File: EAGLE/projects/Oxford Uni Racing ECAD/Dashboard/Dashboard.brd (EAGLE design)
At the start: 165.1 x 153.3 mm, 18 parts, among them J1 T821108A1S100CEU, J2 CAN_OUT, J3 PWR_CAN, K1 EC2-12NU, K2 EC2-12NU, X2 D-SUB9-H2M09ST

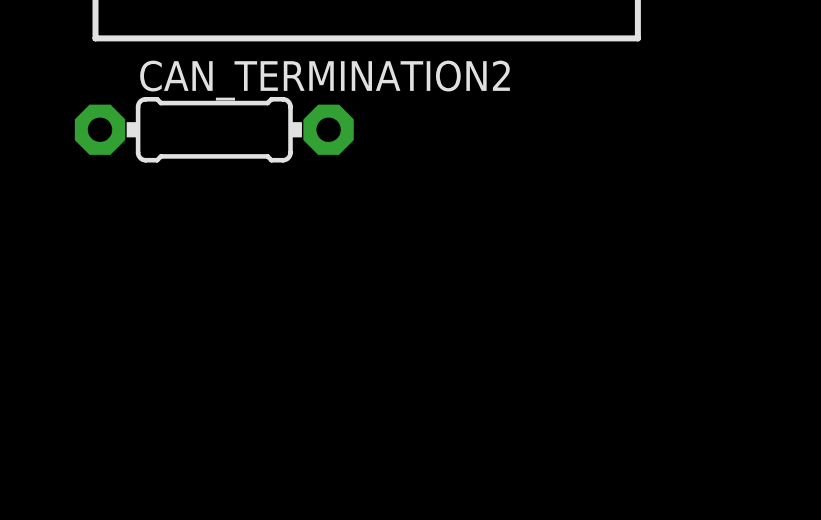
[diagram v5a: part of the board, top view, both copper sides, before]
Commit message: added DISPLAY OUT to dashboard
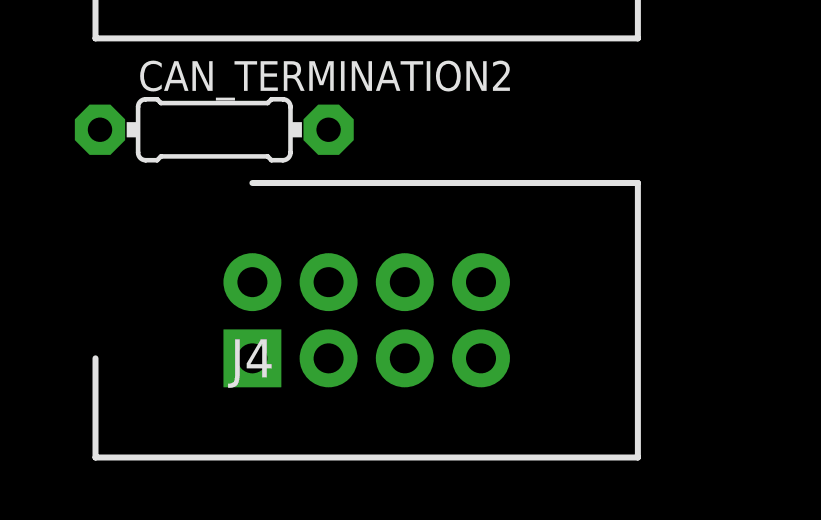
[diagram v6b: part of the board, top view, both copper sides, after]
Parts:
- added J4: DISPL, T821108A1S100CEU:HDRV8W64P254_2X4_1778X895X915P
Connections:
- new net DISPL_SCL: J4.7
- new net DISPL_SDA: J4.5
- net 5V: now also J4.1
- net GND: now also J4.3
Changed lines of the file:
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@@
 <attribute name="VALUE" x="6.35" y="-45.72" size="1.27" layer="27" align="center"/>
+</element>
+<element name="J4" library="T821108A1S100CEU" package="HDRV8W64P254_2X4_1778X895X915P" value="DISPL" x="6.35" y="-59.69" smashed="yes">
+<attribute name="DESCRIPTION" value="HEADER, VERTICAL, 2.54MM, 8WAY Amphenol T821 Series, 2.54mm Pitch 8 Way 2 Row Straight PCB Header, Solder Termination, 3A" x="6.35" y="-59.69" size="1.778" layer="27" display="off"/>
+<attribute name="HEIGHT" value="9.15mm" x="6.35" y="-59.69" size="1.778" layer="27" display="off"/>
+<attribute name="MANUFACTURER_NAME" value="Amphenol" x="6.35" y="-59.69" size="1.778" layer="27" display="off"/>
+<attribute name="MANUFACTURER_PART_NUMBER" value="T821108A1S100CEU" x="6.35" y="-59.69" size="1.778" layer="27" display="off"/>
+<attribute name="NAME" x="6.35" y="-59.69" size="1.27" layer="25" align="center"/>
+<attribute name="RS_PART_NUMBER" value="1702738" x="6.35" y="-59.69" size="1.778" layer="27" display="off"/>
+<attribute name="VALUE" x="6.35" y="-59.69" size="1.27" layer="27" align="center"/>
 </element>
 </elements>
@@
 <contactref element="J2" pad="4"/>
 <contactref element="J2" pad="3"/>
+<contactref element="J4" pad="3"/>
 <wire x1="120.65" y1="16.51" x2="132.08" y2="8.89" width="0" layer="19" extent="16-16"/>
 <wire x1="101.6" y1="11.43" x2="111.76" y2="8.89" width="0" layer="19" extent="16-16"/>
@@
 <wire x1="8.89" y1="-43.18" x2="7.62" y2="-27.94" width="0" layer="19" extent="1-1"/>
 <wire x1="8.89" y1="-45.72" x2="8.89" y2="-43.18" width="0" layer="19" extent="1-1"/>
+<wire x1="8.89" y1="-59.69" x2="8.89" y2="-45.72" width="0" layer="19" extent="1-1"/>
 </signal>
 <signal name="DRIVERSWITCH-">
@@
 <contactref element="J2" pad="1"/>
 <contactref element="J2" pad="2"/>
+<contactref element="J4" pad="1"/>
 <wire x1="88.5571" y1="11.5824" x2="143.51" y2="13.97" width="0" layer="19" extent="1-1"/>
 <wire x1="6.35" y1="-43.18" x2="88.5571" y2="11.5824" width="0" layer="19" extent="1-1"/>
 <wire x1="6.35" y1="-45.72" x2="6.35" y2="-43.18" width="0" layer="19" extent="1-1"/>
+<wire x1="6.35" y1="-59.69" x2="6.35" y2="-45.72" width="0" layer="19" extent="1-1"/>
 </signal>
 <signal name="N$2">
@@
 <wire x1="146.05" y1="12.7" x2="146.05" y2="10.16" width="1.27" layer="16"/>
 </signal>
+<signal name="DISPL_SDA">
+<contactref element="J4" pad="5"/>
+</signal>
+<signal name="DISPL_SCL">
+<contactref element="J4" pad="7"/>
+</signal>
 </signals>

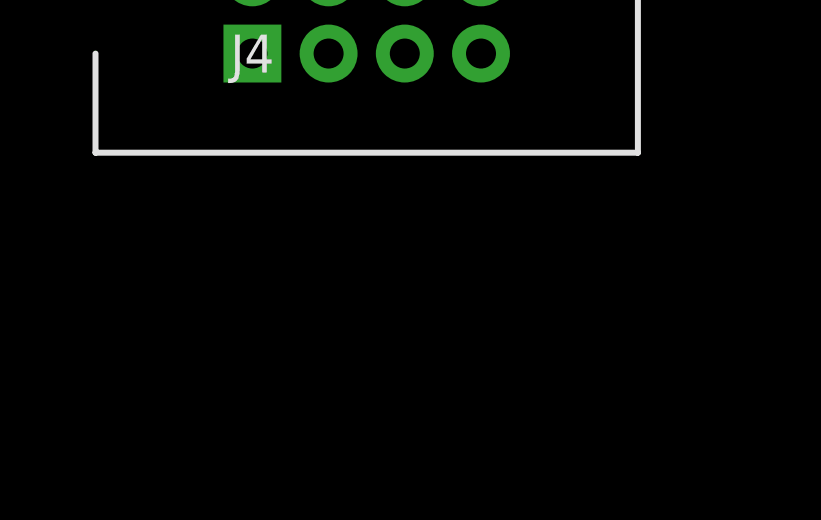
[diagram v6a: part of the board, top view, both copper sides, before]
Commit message: added Buttons OUT to dashboard
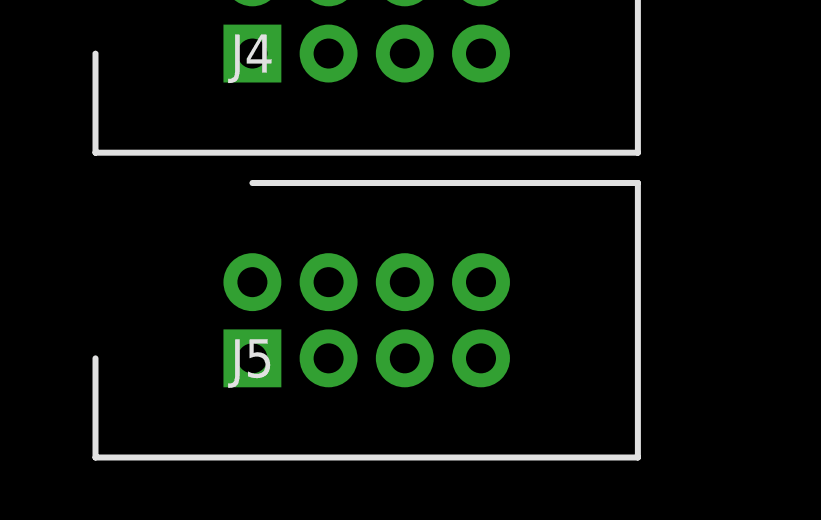
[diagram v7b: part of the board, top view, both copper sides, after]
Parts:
- added J5: DISPL, T821108A1S100CEU:HDRV8W64P254_2X4_1778X895X915P
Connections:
- new net BRAKE_BIAS: J5.6
- new net DRIVER_SELECT: J5.1
- new net EMERGENCY_STOP: J5.7
- new net EVENT_SELECT: J5.3
- new net IGNITION_SWITCH: J5.5
- new net PEDAL_MAPPING: J5.4
- new net PWR_REDUCTION: J5.2
- new net TCS_ON/OFF: J5.8
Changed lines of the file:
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@@
 <attribute name="VALUE" x="6.35" y="-59.69" size="1.27" layer="27" align="center"/>
+</element>
+<element name="J5" library="T821108A1S100CEU" package="HDRV8W64P254_2X4_1778X895X915P" value="DISPL" x="6.35" y="-69.85" smashed="yes">
+<attribute name="DESCRIPTION" value="HEADER, VERTICAL, 2.54MM, 8WAY Amphenol T821 Series, 2.54mm Pitch 8 Way 2 Row Straight PCB Header, Solder Termination, 3A" x="6.35" y="-69.85" size="1.778" layer="27" display="off"/>
+<attribute name="HEIGHT" value="9.15mm" x="6.35" y="-69.85" size="1.778" layer="27" display="off"/>
+<attribute name="MANUFACTURER_NAME" value="Amphenol" x="6.35" y="-69.85" size="1.778" layer="27" display="off"/>
+<attribute name="MANUFACTURER_PART_NUMBER" value="T821108A1S100CEU" x="6.35" y="-69.85" size="1.778" layer="27" display="off"/>
+<attribute name="NAME" x="6.35" y="-69.85" size="1.27" layer="25" align="center"/>
+<attribute name="RS_PART_NUMBER" value="1702738" x="6.35" y="-69.85" size="1.778" layer="27" display="off"/>
+<attribute name="VALUE" x="6.35" y="-69.85" size="1.27" layer="27" align="center"/>
 </element>
 </elements>
@@
 <contactref element="J4" pad="7"/>
 </signal>
+<signal name="DRIVER_SELECT">
+<contactref element="J5" pad="1"/>
+</signal>
+<signal name="EVENT_SELECT">
+<contactref element="J5" pad="3"/>
+</signal>
+<signal name="IGNITION_SWITCH">
+<contactref element="J5" pad="5"/>
+</signal>
+<signal name="EMERGENCY_STOP">
+<contactref element="J5" pad="7"/>
+</signal>
+<signal name="PWR_REDUCTION">
+<contactref element="J5" pad="2"/>
+</signal>
+<signal name="PEDAL_MAPPING">
+<contactref element="J5" pad="4"/>
+</signal>
+<signal name="BRAKE_BIAS">
+<contactref element="J5" pad="6"/>
+</signal>
+<signal name="TCS_ON/OFF">
+<contactref element="J5" pad="8"/>
+</signal>
 </signals>

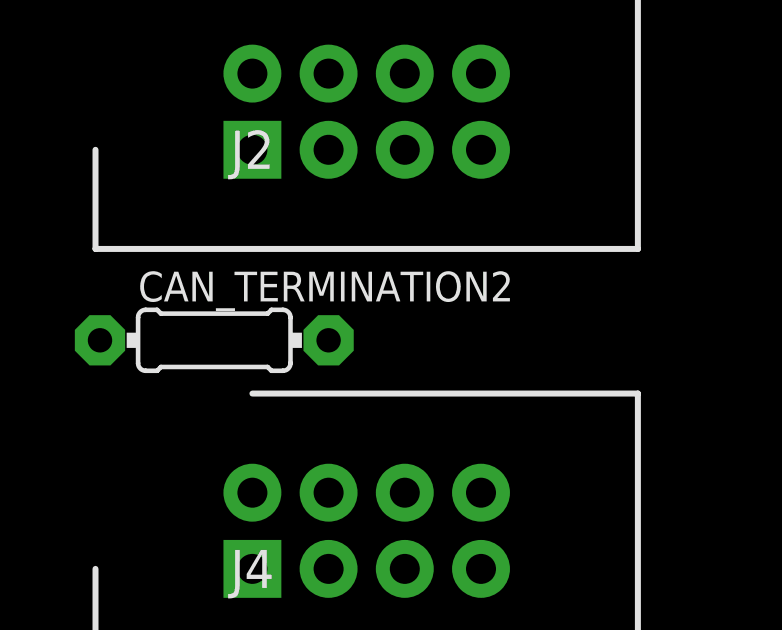
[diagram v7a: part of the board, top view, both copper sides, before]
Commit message: removed redundant CAN termination resistor from dashboard
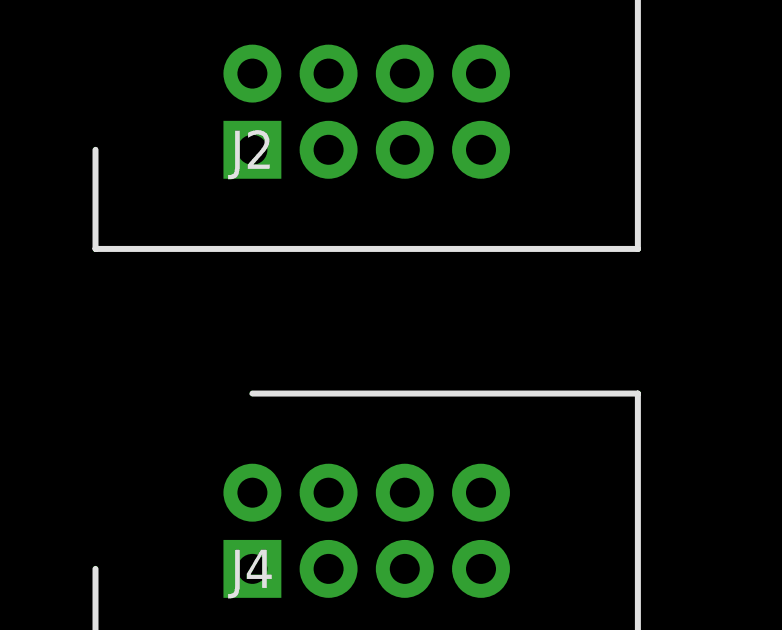
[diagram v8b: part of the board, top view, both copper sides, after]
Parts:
- removed CAN_TERMINATION2: 120, adafruit:0204/7
- J5: value DISPL -> BUTTONS
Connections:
- net CANH: no longer CAN_TERMINATION2.2
- net CANL: no longer CAN_TERMINATION2.1
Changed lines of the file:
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@@
 <attribute name="VALUE" x="144.399" y="16.764" size="1.27" layer="27" ratio="10" rot="R180"/>
-</element>
-<element name="CAN_TERMINATION2" library="adafruit" library_urn="urn:adsk.eagle:library:420" package="0204/7" package3d_urn="urn:adsk.eagle:package:6240596/1" value="120" x="5.08" y="-52.07" smashed="yes">
-<attribute name="NAME" x="2.54" y="-50.7746" size="0.9906" layer="25" ratio="12"/>
-<attribute name="VALUE" x="3.4544" y="-52.5526" size="0.9906" layer="27" ratio="12"/>
 </element>
 <element name="J2" library="T821108A1S100CEU" package="HDRV8W64P254_2X4_1778X895X915P" value="CAN_OUT" x="6.35" y="-45.72" smashed="yes">
@@
 <attribute name="VALUE" x="6.35" y="-59.69" size="1.27" layer="27" align="center"/>
 </element>
-<element name="J5" library="T821108A1S100CEU" package="HDRV8W64P254_2X4_1778X895X915P" value="DISPL" x="6.35" y="-69.85" smashed="yes">
+<element name="J5" library="T821108A1S100CEU" package="HDRV8W64P254_2X4_1778X895X915P" value="BUTTONS" x="6.35" y="-69.85" smashed="yes">
 <attribute name="DESCRIPTION" value="HEADER, VERTICAL, 2.54MM, 8WAY Amphenol T821 Series, 2.54mm Pitch 8 Way 2 Row Straight PCB Header, Solder Termination, 3A" x="6.35" y="-69.85" size="1.778" layer="27" display="off"/>
 <attribute name="HEIGHT" value="9.15mm" x="6.35" y="-69.85" size="1.778" layer="27" display="off"/>
@@
 <wire x1="95.4786" y1="8.7376" x2="95.37065" y2="8.84555" width="0.6096" layer="16"/>
 <wire x1="95.37065" y1="8.84555" x2="95.37065" y2="13.97" width="0.6096" layer="16"/>
-<contactref element="CAN_TERMINATION2" pad="1"/>
+<contactref element="J2" pad="6"/>
 <contactref element="J2" pad="5"/>
-<contactref element="J2" pad="6"/>
 <wire x1="95.25" y1="20.32" x2="95.25" y2="22.86" width="0" layer="19" extent="1-1"/>
 <wire x1="11.43" y1="-43.18" x2="95.37065" y2="8.84555" width="0" layer="19" extent="16-16"/>
 <wire x1="11.43" y1="-45.72" x2="11.43" y2="-43.18" width="0" layer="19" extent="1-1"/>
-<wire x1="1.27" y1="-52.07" x2="11.43" y2="-45.72" width="0" layer="19" extent="1-1"/>
 </signal>
 <signal name="CANH">
@@
 <wire x1="92.71" y1="22.86" x2="87.63" y2="27.94" width="1.27" layer="16"/>
 <wire x1="87.63" y1="27.94" x2="87.63" y2="29.21" width="1.27" layer="16"/>
-<contactref element="CAN_TERMINATION2" pad="2"/>
+<contactref element="J2" pad="8"/>
 <contactref element="J2" pad="7"/>
-<contactref element="J2" pad="8"/>
 <wire x1="13.97" y1="-43.18" x2="92.71" y2="12.9667" width="0" layer="19" extent="16-16"/>
 <wire x1="13.97" y1="-45.72" x2="13.97" y2="-43.18" width="0" layer="19" extent="1-1"/>
-<wire x1="8.89" y1="-52.07" x2="13.97" y2="-45.72" width="0" layer="19" extent="1-1"/>
 </signal>
 <signal name="5V">
